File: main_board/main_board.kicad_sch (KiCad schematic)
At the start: 56 parts, among them J1 USB4105-GF-A-060, J2 Conn_01x06_Pin, Q3 NX3008PBK,215, U1 SSD1306, U2 ESP32-S2-SOLO, U3 TLV62568PDRLT, U4 MCP73832, U5 DW01, U6 8205A, U7 MAX17055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

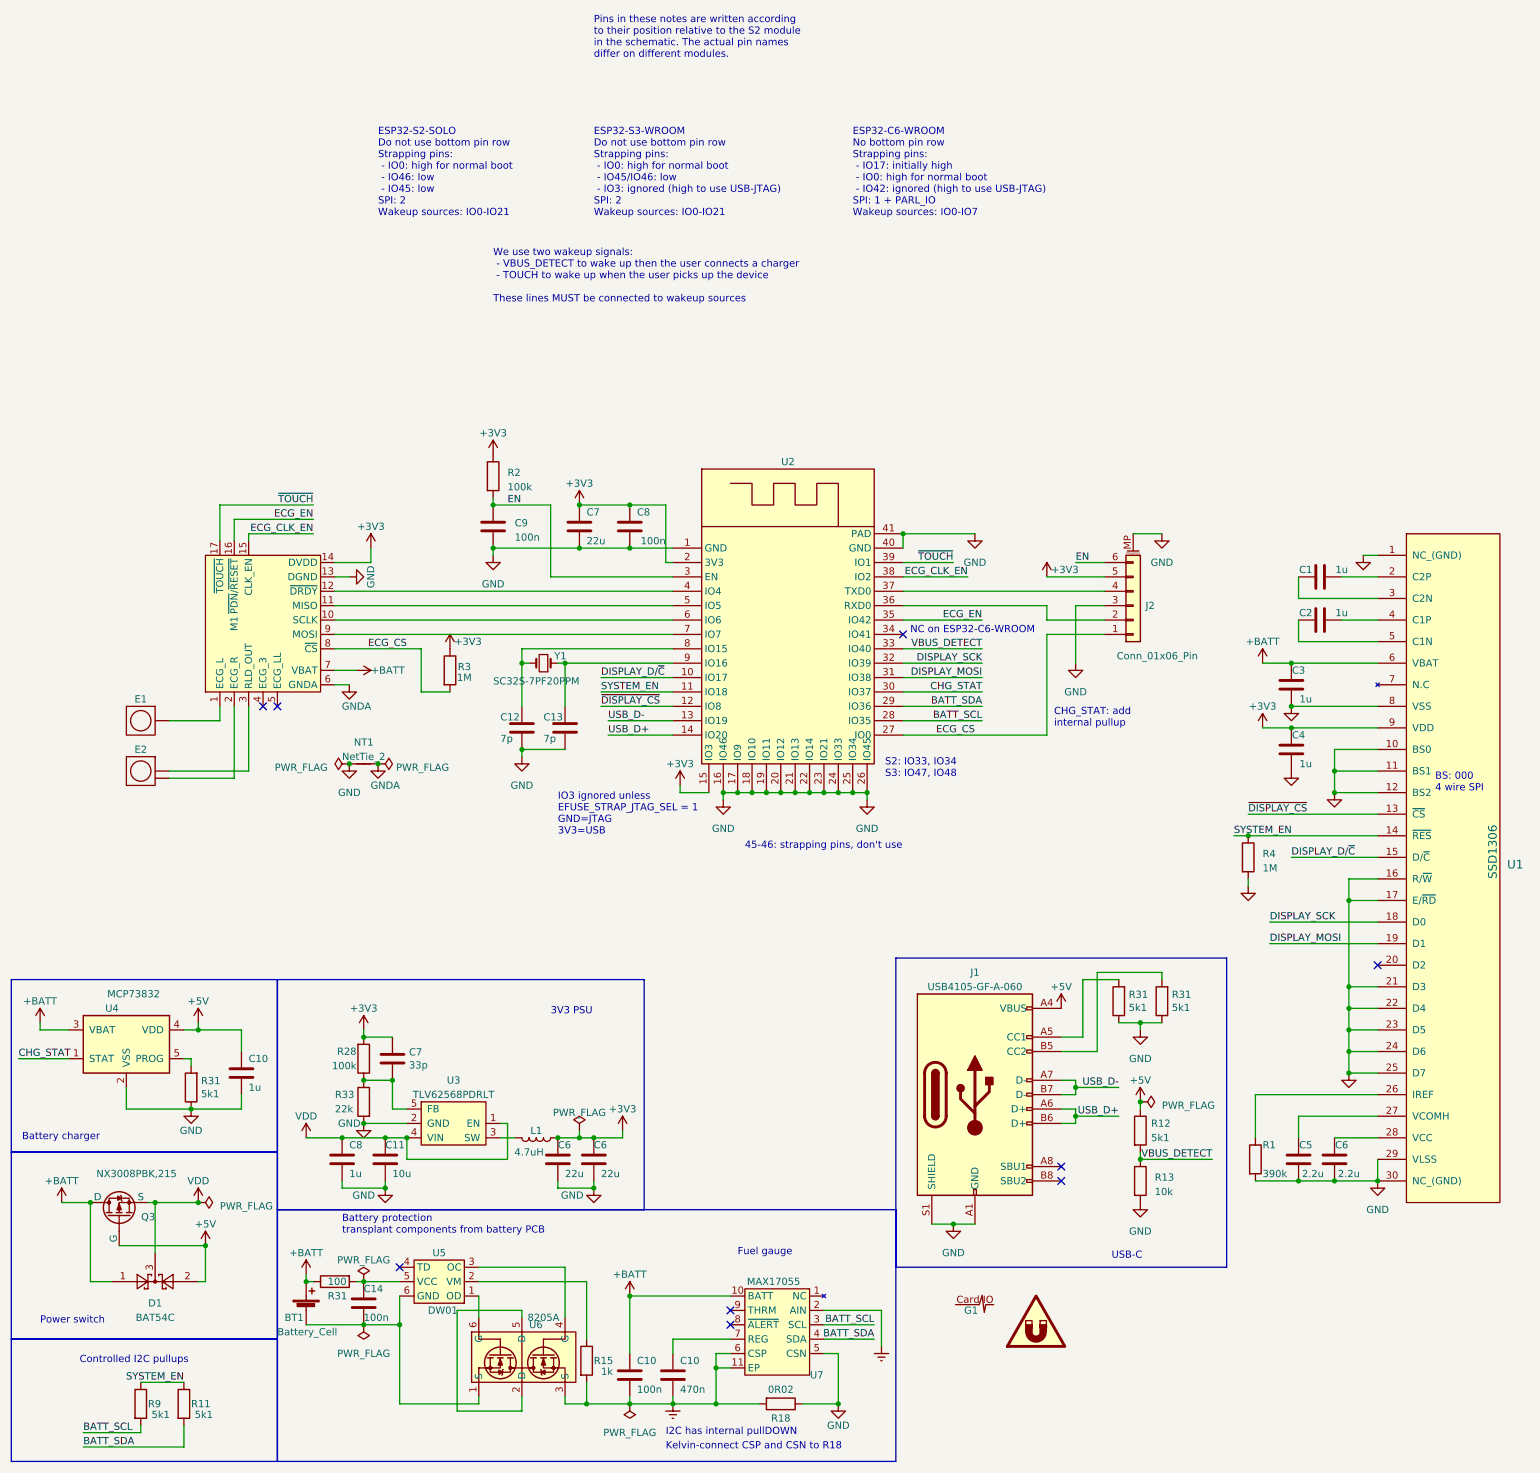
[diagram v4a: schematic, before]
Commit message: Keep fuel gauge comm lines pulled up
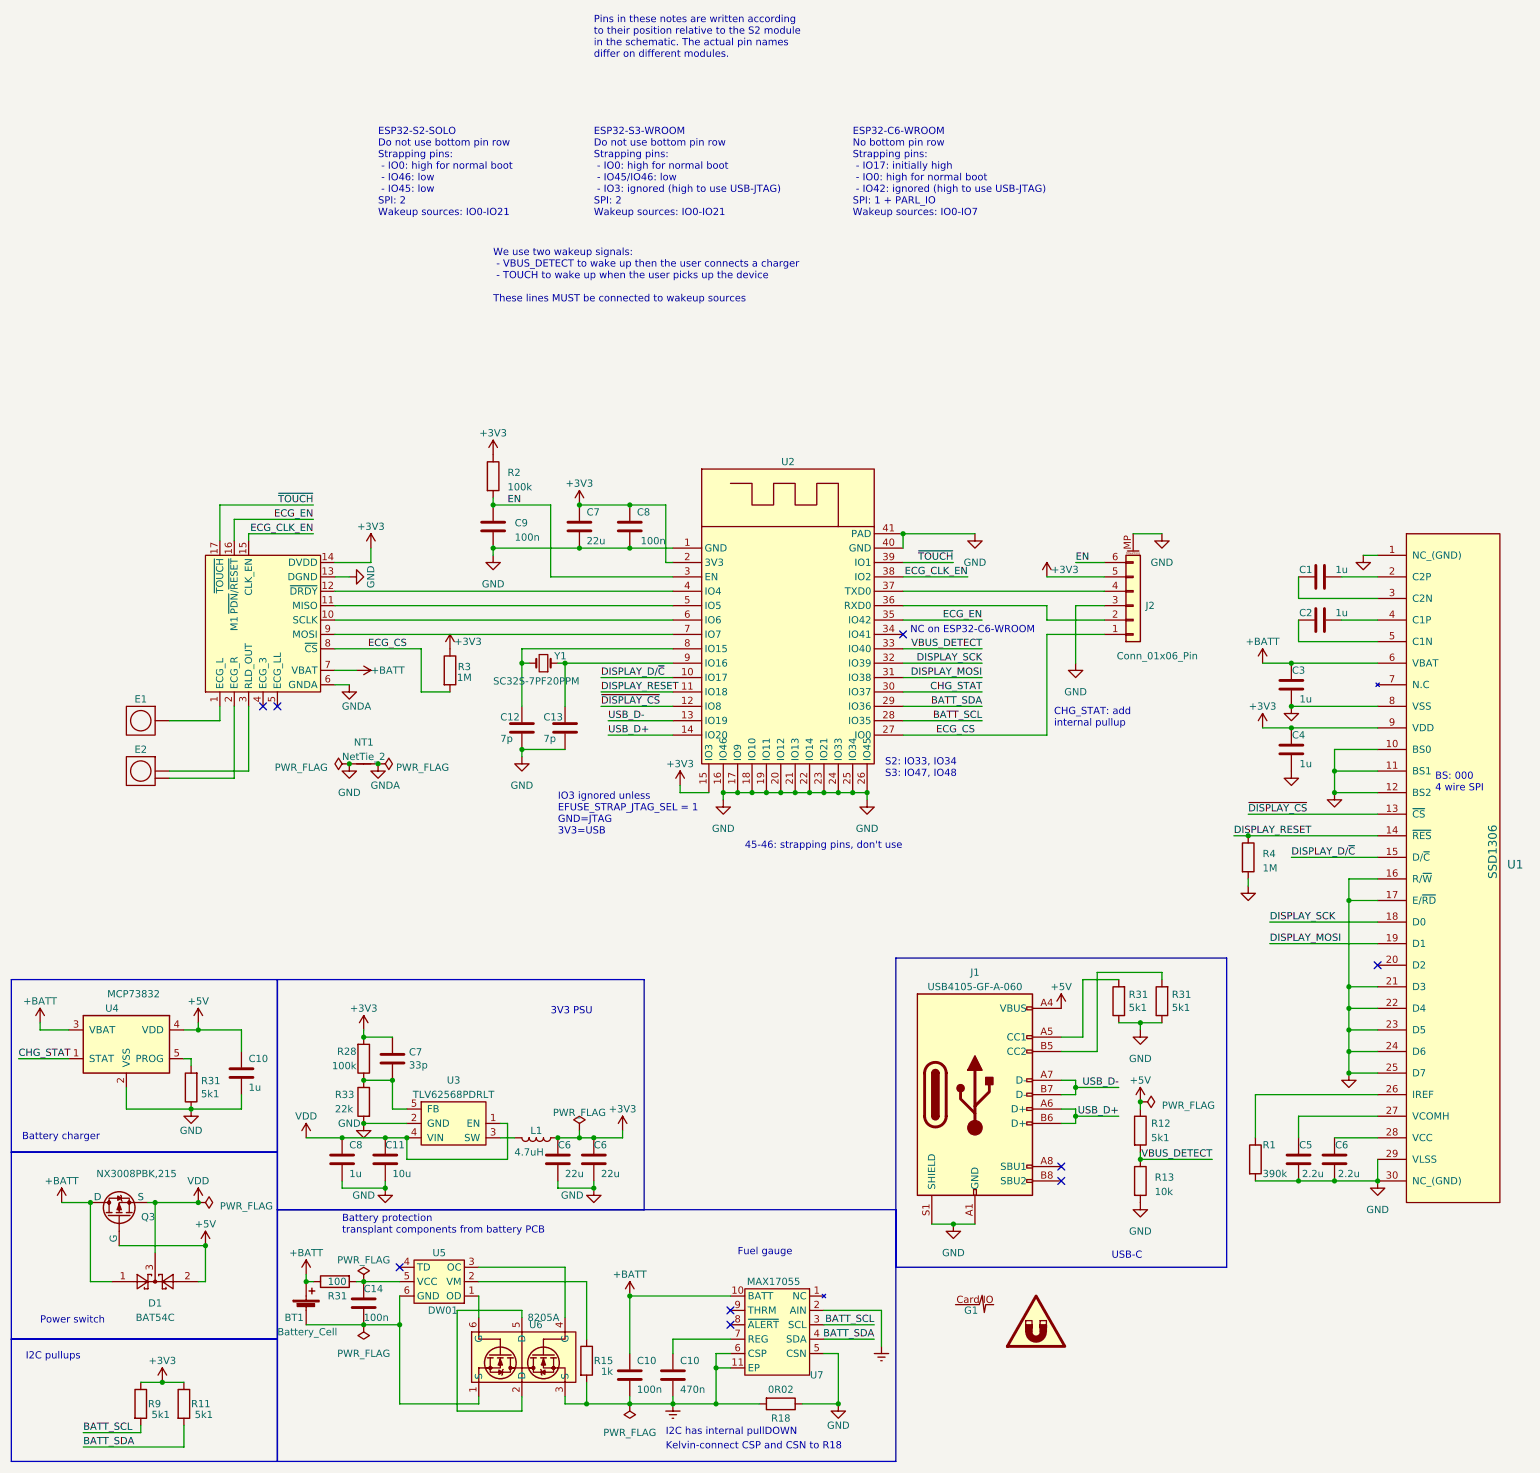
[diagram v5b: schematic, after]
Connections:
- net +3V3: now also R11.1, R9.1
- net SYSTEM_EN renamed DISPLAY_RESET
- net DISPLAY_RESET: no longer R11.1, R9.1
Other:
- note added: "I2C pullups"
- note removed: "Controlled I2C pullups"
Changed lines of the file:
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@@
   (title_block
     (title "Card/IO ECG main board")
-    (date "2023-11-05")
+    (date "2023-11-17")
     (rev "6")
   )
@@
   (junction (at 153.67 78.74) (diameter 0) (color 0 0 0 0)
   )
+  (junction (at 39.37 182.88) (diameter 0) (color 0 0 0 0)
+  )
   (junction (at 246.38 147.32) (diameter 0) (color 0 0 0 0)
   )
@@
     (stroke (width 0) (type default))
   )
+  (wire (pts (xy 39.37 182.88) (xy 43.18 182.88))
+    (stroke (width 0) (type default))
+  )
   (wire (pts (xy 13.97 125.73) (xy 22.86 125.73))
     (stroke (width 0) (type default))
@@
     (stroke (width 0) (type default))
   )
-  (wire (pts (xy 35.56 182.88) (xy 43.18 182.88))
+  (wire (pts (xy 35.56 182.88) (xy 39.37 182.88))
     (stroke (width 0) (type default))
   )
@@
     (effects (font (size 1.27 1.27)) (justify left bottom))
   )
-  (text "Controlled I2C pullups" (at 24.765 179.705 0)
-    (effects (font (size 1.27 1.27)) (justify left bottom))
-  )
   (text "ESP32-C6-WROOM\nNo bottom pin row\nStrapping pins:\n - IO17: initially high\n - IO0: high for normal boot\n - IO42: ignored (high to use USB-JTAG)\nSPI: 1 + PARL_IO\nWakeup sources: IO0-IO7"
     (at 161.29 -22.86 0)
@@
     (effects (font (size 1.27 1.27)) (justify left bottom))
   )
+  (text "I2C pullups" (at 15.24 179.07 0)
+    (effects (font (size 1.27 1.27)) (justify left bottom))
+  )
   (text "IO3 ignored unless\nEFUSE_STRAP_JTAG_SEL = 1\nGND=JTAG\n3V3=USB"
     (at 109.22 86.36 0)
@@
     (effects (font (size 1.27 1.27)) (justify left bottom))
   )
-  (label "SYSTEM_EN" (at 116.84 60.96 0) (fields_autoplaced)
+  (label "DISPLAY_RESET" (at 116.84 60.96 0) (fields_autoplaced)
+    (effects (font (size 1.27 1.27)) (justify left bottom))
+  )
+  (label "DISPLAY_RESET" (at 228.6 86.36 0) (fields_autoplaced)
     (effects (font (size 1.27 1.27)) (justify left bottom))
   )
@@
     (effects (font (size 1.27 1.27)) (justify left bottom))
   )
-  (label "SYSTEM_EN" (at 228.6 86.36 0) (fields_autoplaced)
-    (effects (font (size 1.27 1.27)) (justify left bottom))
-  )
   (label "DISPLAY_D{slash}~{C}" (at 116.84 58.42 0) (fields_autoplaced)
     (effects (font (size 1.27 1.27)) (justify left bottom))
@@
     (effects (font (size 1.27 1.27)) (justify right bottom))
   )
-  (label "SYSTEM_EN" (at 43.18 182.88 180) (fields_autoplaced)
-    (effects (font (size 1.27 1.27)) (justify right bottom))
-  )
   (label "BATT_SCL" (at 184.15 66.04 180) (fields_autoplaced)
     (effects (font (size 1.27 1.27)) (justify right bottom))
@@
         )
       )
+    )
+  )
+  (symbol (lib_id "power:+3V3") (at 39.37 182.88 0) (unit 1)
+    (in_bom yes) (on_board yes) (dnp no) (fields_autoplaced)
+    (property "Reference" "#PWR045" (at 39.37 186.69 0)
+      (effects (font (size 1.27 1.27)) hide)
+    )
+    (property "Value" "+3V3" (at 39.37 179.07 0)
+      (effects (font (size 1.27 1.27)))
+    )
+    (property "Footprint" "" (at 39.37 182.88 0)
+      (effects (font (size 1.27 1.27)) hide)
+    )
+    (property "Datasheet" "" (at 39.37 182.88 0)
+      (effects (font (size 1.27 1.27)) hide)
+    )
+    (pin "1")
+    (instances
+      (project "main_board"
+        (path "/e55848cd-275a-4b5e-8e68-b5d8d07c8d31"
+          (reference "#PWR045") (unit 1)
+        )
+      )

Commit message: Label the serial debug port, add strapping pullup
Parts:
- added R5: 1M, Resistor_SMD:R_0603_1608Metric, symbol Device:R
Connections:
- net +3V3: now also R5.1
- net ~{DISPLAY_CS}: now also R5.2
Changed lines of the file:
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@@
+    (stroke (width 0) (type default))
+  )
+  (wire (pts (xy 226.06 82.55) (xy 254 82.55))
     (stroke (width 0) (type default))
   )
@@
   )
   (wire (pts (xy 248.92 124.46) (xy 254 124.46))
-    (stroke (width 0) (type default))
-  )
-  (wire (pts (xy 231.14 82.55) (xy 254 82.55))
     (stroke (width 0) (type default))
   )
@@
     )
   )
+  (symbol (lib_id "power:+3V3") (at 226.06 74.93 0) (mirror y) (unit 1)
+    (in_bom yes) (on_board yes) (dnp no) (fields_autoplaced)
+    (property "Reference" "#PWR051" (at 226.06 78.74 0)
+      (effects (font (size 1.27 1.27)) hide)
+    )
+    (property "Value" "+3V3" (at 226.06 71.12 0)
+      (effects (font (size 1.27 1.27)))
+    )
+    (property "Footprint" "" (at 226.06 74.93 0)
+      (effects (font (size 1.27 1.27)) hide)
+    )
+    (property "Datasheet" "" (at 226.06 74.93 0)
+      (effects (font (size 1.27 1.27)) hide)
+    )
+    (pin "1")
+    (instances
+      (project "main_board"
+        (path "/e55848cd-275a-4b5e-8e68-b5d8d07c8d31"
+          (reference "#PWR051") (unit 1)
+        )
+      )
+    )
+  )
   (symbol (lib_id "power:GND") (at 254 147.32 0) (unit 1)
     (in_bom yes) (on_board yes) (dnp no) (fields_autoplaced)
@@
         )
       )
+    )
+  )
+  (symbol (lib_id "Device:R") (at 226.06 78.74 0) (unit 1)
+    (in_bom yes) (on_board yes) (dnp no) (fields_autoplaced)
+    (property "Reference" "R5" (at 228.6 78.105 0)
+      (effects (font (size 1.27 1.27)) (justify left))
+    )
+    (property "Value" "1M" (at 228.6 80.645 0)
+      (effects (font (size 1.27 1.27)) (justify left))
+    )
+    (property "Footprint" "Resistor_SMD:R_0603_1608Metric" (at 224.282 78.74 90)
+      (effects (font (size 1.27 1.27)) hide)
+    )
+    (property "Datasheet" "~" (at 226.06 78.74 0)
+      (effects (font (size 1.27 1.27)) hide)
+    )
+    (pin "1")
+    (pin "2")
+    (instances
+      (project "main_board"
+        (path "/e55848cd-275a-4b5e-8e68-b5d8d07c8d31"
+          (reference "R5") (unit 1)
+        )
+      )

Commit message: Pull up D/C instead of CS
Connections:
- net DISPLAY_D/~{C}: now also R5.2
- net ~{DISPLAY_CS}: no longer R5.2
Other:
- moved on the sheet: R4, R5
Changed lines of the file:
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@@
   (junction (at 238.76 55.88) (diameter 0) (color 0 0 0 0)
   )
-  (junction (at 231.14 86.36) (diameter 0) (color 0 0 0 0)
-  )
   (junction (at 45.72 151.13) (diameter 0) (color 0 0 0 0)
   )
@@
     (stroke (width 0) (type default))
   )
-  (wire (pts (xy 226.06 82.55) (xy 254 82.55))
+  (wire (pts (xy 233.68 82.55) (xy 254 82.55))
     (stroke (width 0) (type default))
   )
@@
     (stroke (width 0) (type default))
   )
-  (wire (pts (xy 231.14 93.98) (xy 231.14 95.25))
+  (wire (pts (xy 224.79 93.98) (xy 224.79 96.52))
     (stroke (width 0) (type default))
   )
@@
     (stroke (width 0) (type default))
   )
+  (wire (pts (xy 238.76 99.06) (xy 238.76 90.17))
+    (stroke (width 0) (type default))
+  )
   (wire (pts (xy 69.85 38.1) (xy 76.2 38.1))
     (stroke (width 0) (type default))
@@
     (stroke (width 0) (type default))
   )
+  (wire (pts (xy 232.41 99.06) (xy 238.76 99.06))
+    (stroke (width 0) (type default))
+  )
   (wire (pts (xy 248.92 120.65) (xy 248.92 124.46))
     (stroke (width 0) (type default))
@@
     (stroke (width 0) (type default))
   )
-  (wire (pts (xy 228.6 86.36) (xy 231.14 86.36))
-    (stroke (width 0) (type default))
-  )
   (wire (pts (xy 212.09 119.38) (xy 215.9 119.38))
     (stroke (width 0) (type default))
@@
     (stroke (width 0) (type default))
   )
-  (wire (pts (xy 231.14 86.36) (xy 254 86.36))
+  (wire (pts (xy 224.79 86.36) (xy 254 86.36))
     (stroke (width 0) (type default))
   )
@@
     (effects (font (size 1.27 1.27)) (justify right bottom))
   )
-  (label "~{DISPLAY_CS}" (at 231.14 82.55 0) (fields_autoplaced)
+  (label "~{DISPLAY_CS}" (at 233.68 82.55 0) (fields_autoplaced)
     (effects (font (size 1.27 1.27)) (justify left bottom))
   )
@@
     )
   )
-  (symbol (lib_id "power:+3V3") (at 226.06 74.93 0) (mirror y) (unit 1)
+  (symbol (lib_id "power:+3V3") (at 232.41 91.44 0) (mirror y) (unit 1)
     (in_bom yes) (on_board yes) (dnp no) (fields_autoplaced)
-    (property "Reference" "#PWR051" (at 226.06 78.74 0)
+    (property "Reference" "#PWR051" (at 232.41 95.25 0)
       (effects (font (size 1.27 1.27)) hide)
     )
-    (property "Value" "+3V3" (at 226.06 71.12 0)
+    (property "Value" "+3V3" (at 232.41 87.63 0)
       (effects (font (size 1.27 1.27)))
     )
-    (property "Footprint" "" (at 226.06 74.93 0)
+    (property "Footprint" "" (at 232.41 91.44 0)
       (effects (font (size 1.27 1.27)) hide)
     )
-    (property "Datasheet" "" (at 226.06 74.93 0)
+    (property "Datasheet" "" (at 232.41 91.44 0)
       (effects (font (size 1.27 1.27)) hide)
     )
@@
     )
   )
-  (symbol (lib_id "Device:R") (at 226.06 78.74 0) (unit 1)
+  (symbol (lib_id "Device:R") (at 232.41 95.25 0) (unit 1)
     (in_bom yes) (on_board yes) (dnp no) (fields_autoplaced)
-    (property "Reference" "R5" (at 228.6 78.105 0)
+    (property "Reference" "R5" (at 234.95 94.615 0)
       (effects (font (size 1.27 1.27)) (justify left))
     )
-    (property "Value" "1M" (at 228.6 80.645 0)
+    (property "Value" "1M" (at 234.95 97.155 0)
       (effects (font (size 1.27 1.27)) (justify left))
     )
-    (property "Footprint" "Resistor_SMD:R_0603_1608Metric" (at 224.282 78.74 90)
+    (property "Footprint" "Resistor_SMD:R_0603_1608Metric" (at 230.632 95.25 90)
       (effects (font (size 1.27 1.27)) hide)
     )
-    (property "Datasheet" "~" (at 226.06 78.74 0)
+    (property "Datasheet" "~" (at 232.41 95.25 0)
       (effects (font (size 1.27 1.27)) hide)
     )
@@
     )
   )
-  (symbol (lib_id "power:GND") (at 231.14 95.25 0) (unit 1)
+  (symbol (lib_id "power:GND") (at 224.79 96.52 0) (unit 1)
     (in_bom yes) (on_board yes) (dnp no)
-    (property "Reference" "#PWR024" (at 231.14 101.6 0)
+    (property "Reference" "#PWR024" (at 224.79 102.87 0)
       (effects (font (size 1.27 1.27)) hide)
     )
-    (property "Value" "GND" (at 227.33 96.52 0)
+    (property "Value" "GND" (at 220.98 97.79 0)
       (effects (font (size 1.27 1.27)) hide)
     )
-    (property "Footprint" "" (at 231.14 95.25 0)
+    (property "Footprint" "" (at 224.79 96.52 0)
       (effects (font (size 1.27 1.27)) hide)
     )
-    (property "Datasheet" "" (at 231.14 95.25 0)
+    (property "Datasheet" "" (at 224.79 96.52 0)
       (effects (font (size 1.27 1.27)) hide)
     )
@@
     )
   )
-  (symbol (lib_id "Device:R") (at 231.14 90.17 0) (unit 1)
+  (symbol (lib_id "Device:R") (at 224.79 90.17 0) (unit 1)
     (in_bom yes) (on_board yes) (dnp no) (fields_autoplaced)
-    (property "Reference" "R4" (at 233.68 89.535 0)
+    (property "Reference" "R4" (at 227.33 89.535 0)
       (effects (font (size 1.27 1.27)) (justify left))
     )
-    (property "Value" "1M" (at 233.68 92.075 0)
+    (property "Value" "1M" (at 227.33 92.075 0)
       (effects (font (size 1.27 1.27)) (justify left))
     )
-    (property "Footprint" "Resistor_SMD:R_0603_1608Metric" (at 229.362 90.17 90)
+    (property "Footprint" "Resistor_SMD:R_0603_1608Metric" (at 223.012 90.17 90)
       (effects (font (size 1.27 1.27)) hide)
     )
-    (property "Datasheet" "~" (at 231.14 90.17 0)
+    (property "Datasheet" "~" (at 224.79 90.17 0)
       (effects (font (size 1.27 1.27)) hide)
     )

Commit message: Move VBUS_DETECT to a LP_IO pin
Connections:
- net ECG_CLK_EN: now also U2.33 (IO40); no longer U2.38 (IO2)
- net VBUS_DETECT: now also U2.38 (IO2); no longer U2.33 (IO40)
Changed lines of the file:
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@@
     (stroke (width 0) (type default))
   )
-  (wire (pts (xy 170.18 40.64) (xy 181.61 40.64))
+  (wire (pts (xy 170.18 40.64) (xy 182.88 40.64))
     (stroke (width 0) (type default))
   )
@@
     (effects (font (size 1.27 1.27)) (justify left bottom))
   )
-  (label "VBUS_DETECT" (at 184.15 53.34 180) (fields_autoplaced)
+  (label "VBUS_DETECT" (at 182.88 40.64 180) (fields_autoplaced)
     (effects (font (size 1.27 1.27)) (justify right bottom))
   )
@@
     (effects (font (size 1.27 1.27)) (justify right bottom))
   )
-  (label "ECG_CLK_EN" (at 181.61 40.64 180) (fields_autoplaced)
-    (effects (font (size 1.27 1.27)) (justify right bottom))
-  )
+  (label "ECG_CLK_EN" (at 184.15 53.34 180) (fields_autoplaced)
+    (effects (font (size 1.27 1.27)) (justify right bottom))
+  )
